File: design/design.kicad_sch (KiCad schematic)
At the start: 19 parts, among them J2 Conn_01x08_Socket, SW1 SW_Push, SW10 SW_Push, SW11 SW_Push, SW12 SW_Push, SW13 SW_Push, SW2 SW_Push, SW3 SW_Push, SW4 SW_Push, SW5 SW_Push, SW6 SW_Push, SW7 SW_Push, SW8 SW_Push, SW9 SW_Push

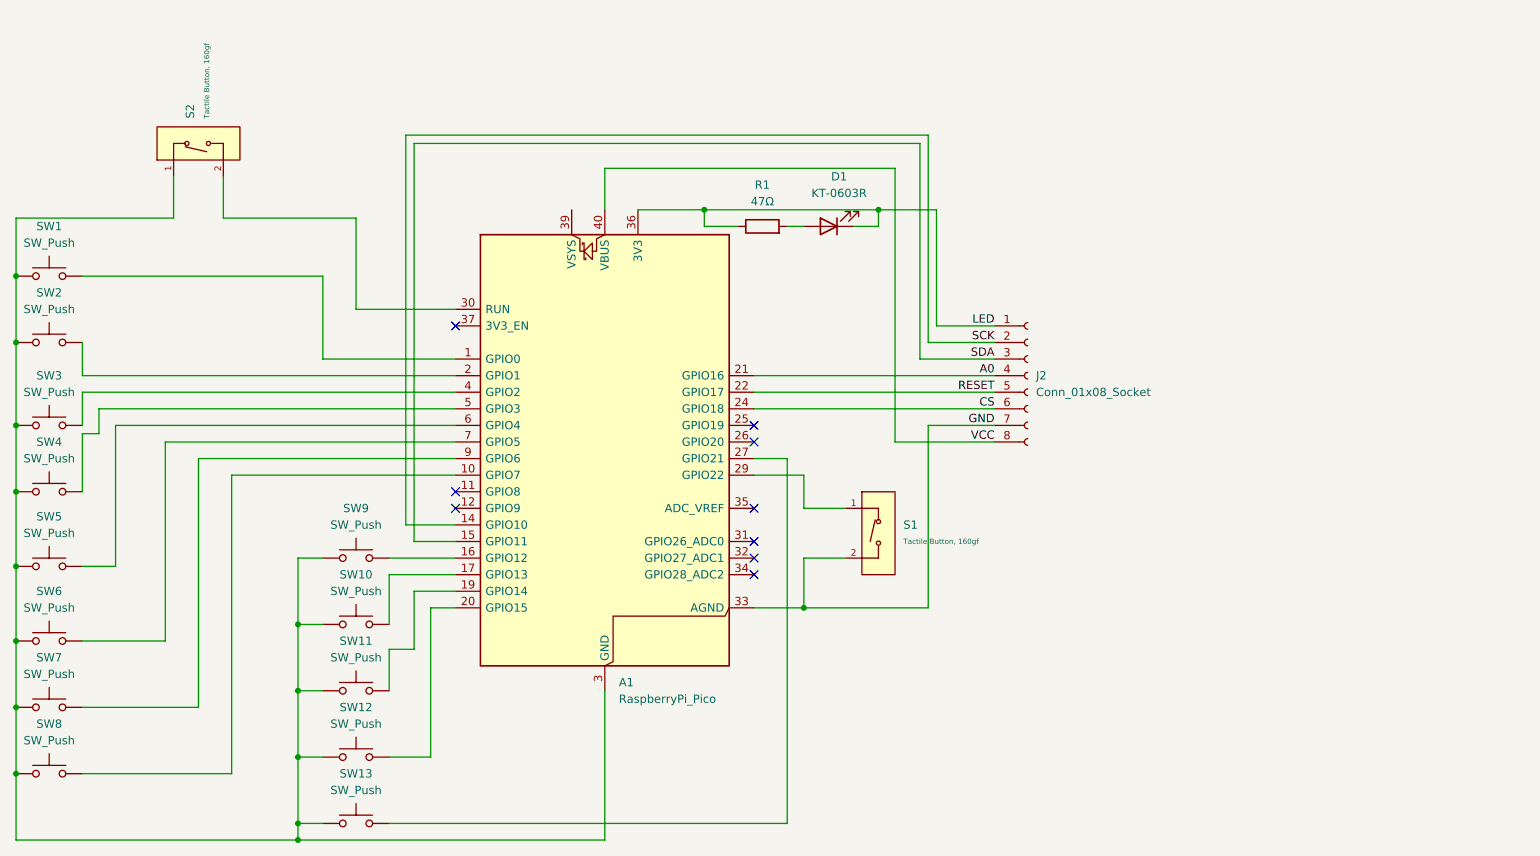
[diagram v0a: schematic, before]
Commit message: Adding gyroscope, redesigning PCB
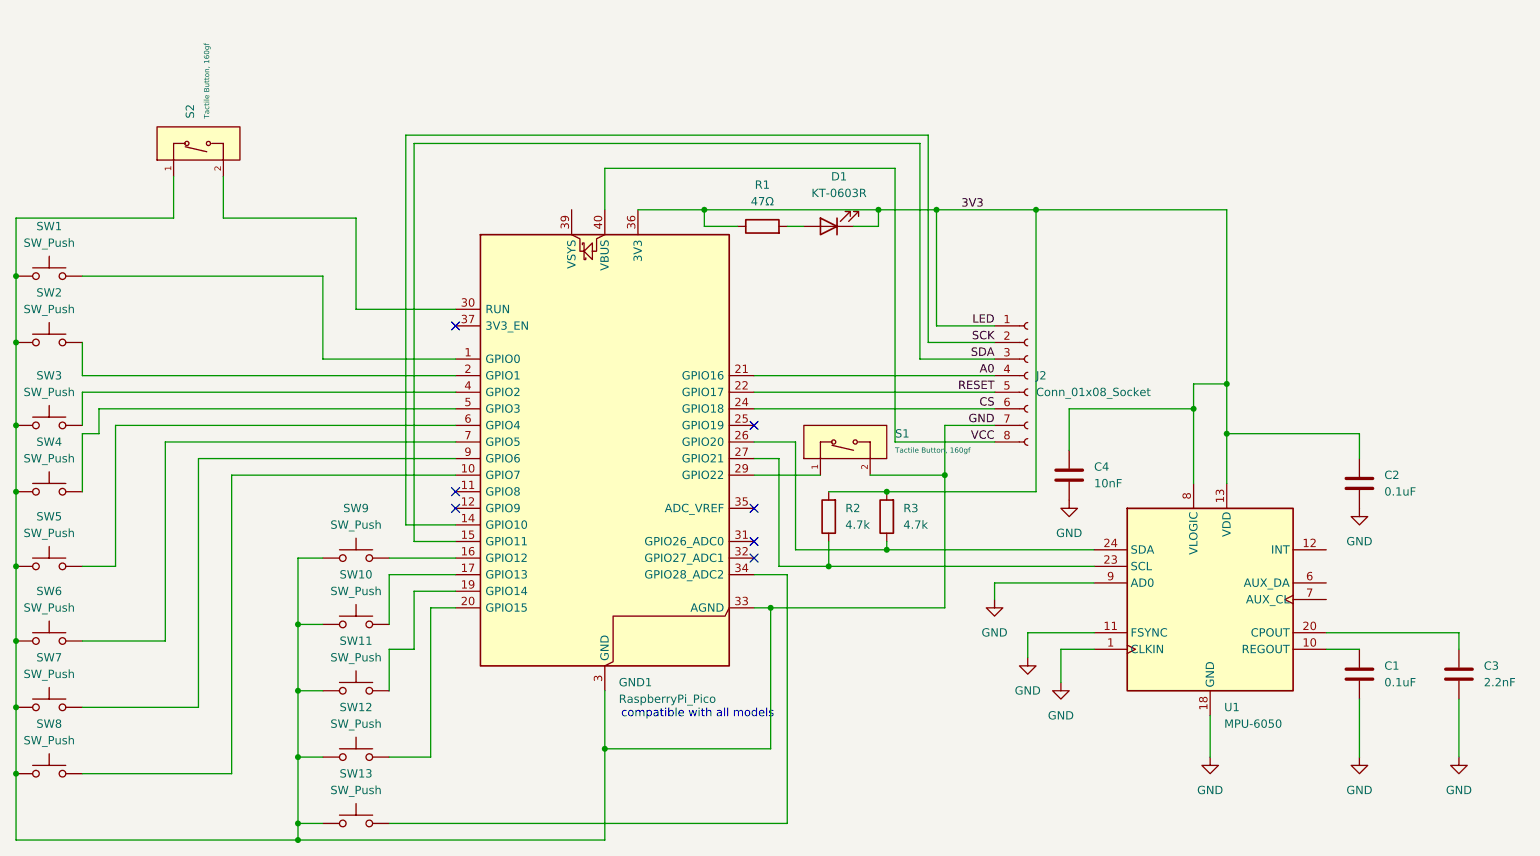
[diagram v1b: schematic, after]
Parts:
- added C1, C2: 0.1uF, Capacitor_SMD:C_0402_1005Metric, symbol Device:C
- added C3: 2.2nF, Capacitor_SMD:C_0603_1608Metric, symbol Device:C
- added C4: 10nF, Capacitor_SMD:C_0603_1608Metric, symbol Device:C
- added R2, R3: 4.7k, Resistor_SMD:R_0603_1608Metric, symbol Device:R
- added U1: MPU-6050, Sensor_Motion:InvenSense_QFN-24_4x4mm_P0.5mm, symbol Sensor_Motion:MPU-6050
- renumbered A1 to GND1
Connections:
- net GND: now also GND1.13 (GND), GND1.18 (GND), GND1.23 (GND), GND1.28 (GND), GND1.3 (GND), GND1.38 (GND), GND1.8 (GND), S2.1 (A), SW1.2, SW10.2, SW11.2, SW12.2, SW13.2, SW2.2, SW3.2, SW4.2, SW5.2, SW6.2, SW7.2, SW8.2, SW9.2, C1.2, C2.2, C3.2, C4.2, U1.1 (CLKIN), U1.11 (FSYNC), U1.18 (GND), U1.9 (AD0)
- net at GND1.26 (GPIO20): now also R3.1, U1.24 (SDA)
- net at GND1.27 (GPIO21): now also R2.1, U1.23 (SCL); no longer SW13.1
- net at GND1.34 (GPIO28_ADC2): now also SW13.1
- net LED renamed 3V3
- net 3V3: now also C2.1, C4.1, R2.2, R3.2, U1.13 (VDD), U1.8 (VLOGIC)
- new net: C3.1, U1.20 (CPOUT)
- new net: C1.1, U1.10 (REGOUT)
- no-connect marks 9 -> 7
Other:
- note added: "compatible with all models"
- moved on the sheet: S1

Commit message: Added details on parts, added gyroscope to design
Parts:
- U1: LCSC (none) -> C24112
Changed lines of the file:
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@@
+			)
+		)
+		(property "LCSC" "C24112"
+			(at 218.44 106.68 0)
+			(hide yes)
+			(show_name no)
+			(do_not_autoplace no)
+			(effects
+				(font
+					(size 1.27 1.27)
+				)
 			)
 		)
